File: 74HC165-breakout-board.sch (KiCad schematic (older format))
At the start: 6 parts, among them J1 Conn_01x05, J2 Conn_01x05

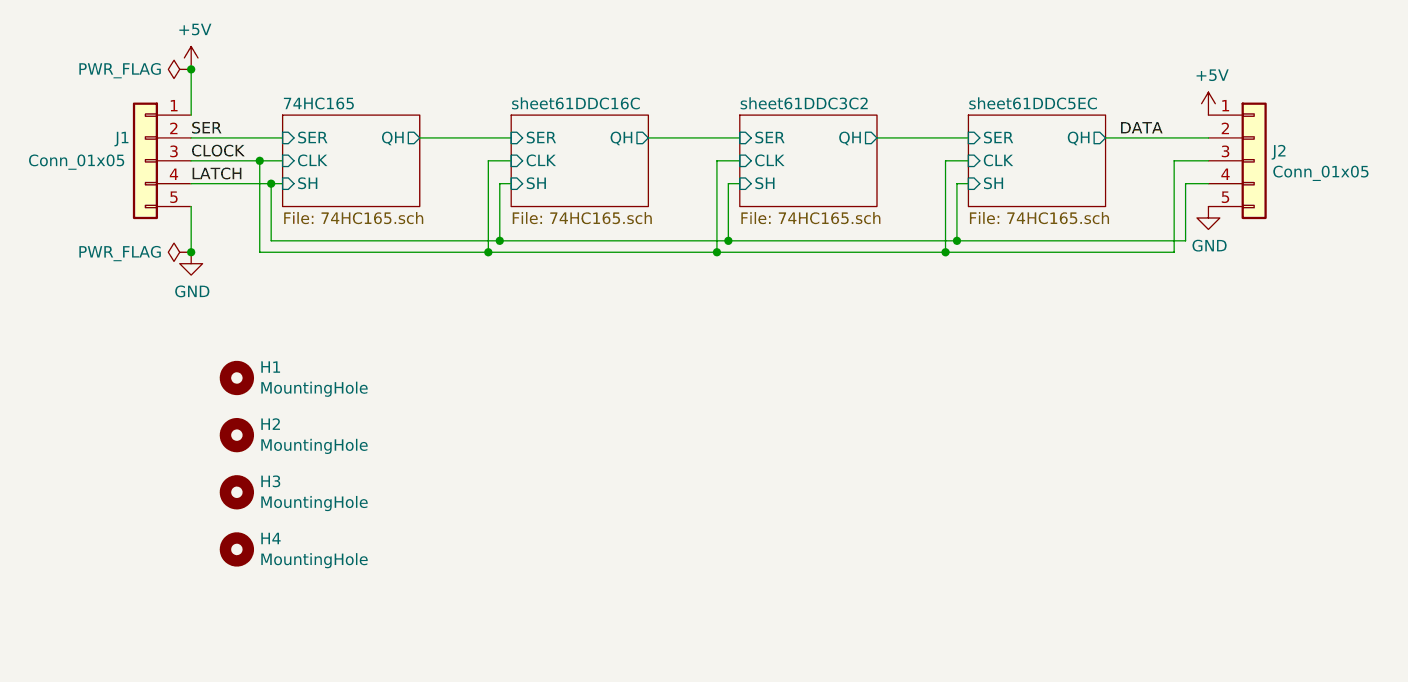
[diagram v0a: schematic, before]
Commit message: Add GND to each header, remove daisy chain
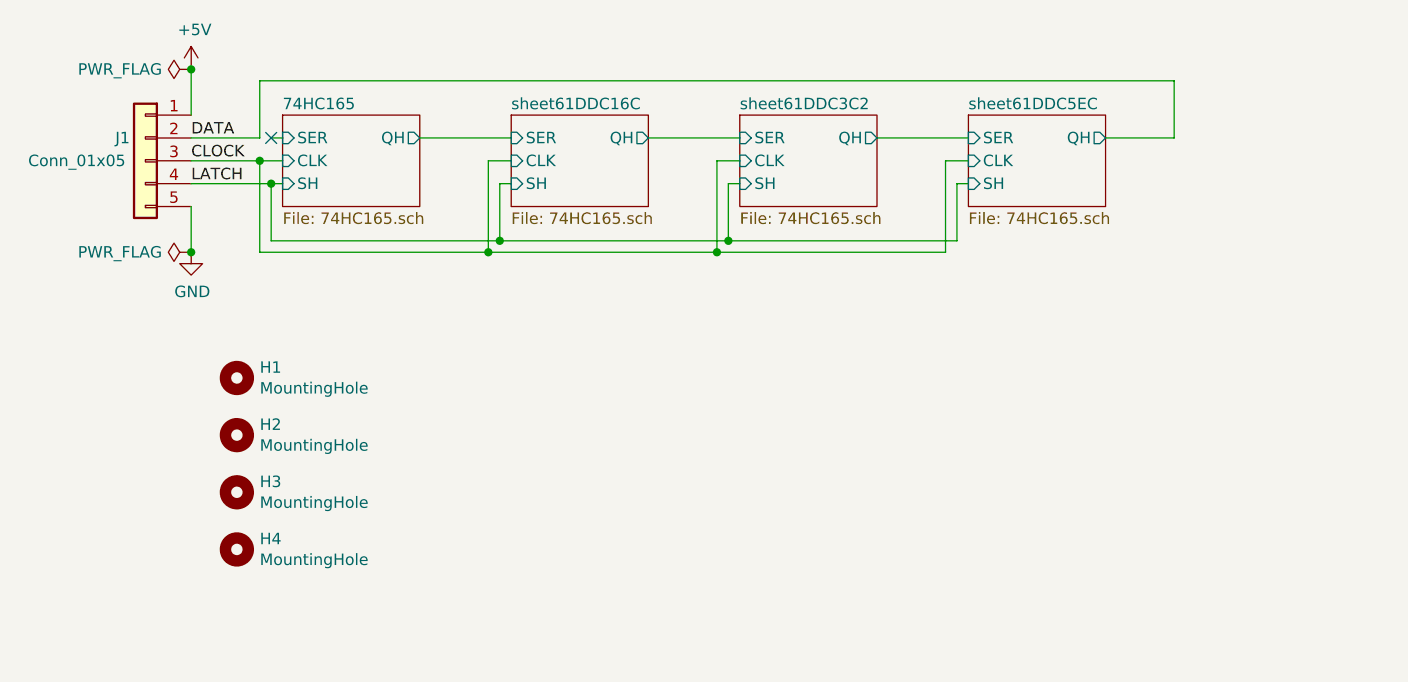
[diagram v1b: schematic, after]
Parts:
- removed J2: Conn_01x05, Connector_JST:JST_XH_B5B-XH-A_1x05_P2.50mm_Vertical, symbol Connector_Generic:Conn_01x05
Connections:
- net SER is gone; now on net DATA: J1.2 (Pin_2)
- no-connect marks 0 -> 1
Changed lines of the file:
@@
 $EndComp
 $Comp
-L power:GND #PWR04
+L power:GND #PWR02
 U 1 1 61DD9981
 P 1300 1500
-F 0 "#PWR04" H 1300 1250 50  0001 C CNN
+F 0 "#PWR02" H 1300 1250 50  0001 C CNN
 F 1 "GND" H 1305 1327 50  0000 C CNN
 F 2 "" H 1300 1500 50  0001 C CNN
@@
 Connection ~ 3600 1500
 $Comp
-L Connector_Generic:Conn_01x05 J2
-U 1 1 61DDF5C9
-P 5950 1100
-F 0 "J2" H 6030 1142 50  0000 L CNN
-F 1 "Conn_01x05" H 6030 1051 50  0000 L CNN
-F 2 "Connector_JST:JST_XH_B5B-XH-A_1x05_P2.50mm_Vertical" H 5950 1100 50  0001 C CNN
-F 3 "~" H 5950 1100 50  0001 C CNN
-	1    5950 1100
-	1    0    0    -1
-$EndComp
-$Comp
-L power:+5V #PWR02
-U 1 1 61DE0AC2
-P 5750 900
-F 0 "#PWR02" H 5750 750 50  0001 C CNN
-F 1 "+5V" H 5765 1073 50  0000 C CNN
-F 2 "" H 5750 900 50  0001 C CNN
-F 3 "" H 5750 900 50  0001 C CNN
-	1    5750 900
-	1    0    0    -1
-$EndComp
-$Comp
-L power:GND #PWR03
-U 1 1 61DE0CBC
-P 5750 1300
-F 0 "#PWR03" H 5750 1050 50  0001 C CNN
-F 1 "GND" H 5755 1127 50  0000 C CNN
-F 2 "" H 5750 1300 50  0001 C CNN
-F 3 "" H 5750 1300 50  0001 C CNN
-	1    5750 1300
-	1    0    0    -1
-$EndComp
-Wire Wire Line
-	4600 1500 5600 1500
-Connection ~ 4600 1500
-Connection ~ 4650 1450
-$Comp
-L power:PWR_FLAG #FLG0101
+L power:PWR_FLAG #FLG01
 U 1 1 61DE2F11
 P 1300 700
-F 0 "#FLG0101" H 1300 775 50  0001 C CNN
+F 0 "#FLG01" H 1300 775 50  0001 C CNN
 F 1 "PWR_FLAG" V 1300 827 50  0000 L CNN
 F 2 "" H 1300 700 50  0001 C CNN
@@
 $EndComp
 Connection ~ 1300 700
-Text Label 5550 1000 2    50   ~ 0
-DATA
-$Comp
-L power:PWR_FLAG #FLG0102
+$Comp
+L power:PWR_FLAG #FLG02
 U 1 1 61DE455D
 P 1300 1500
-F 0 "#FLG0102" H 1300 1575 50  0001 C CNN
+F 0 "#FLG02" H 1300 1575 50  0001 C CNN
 F 1 "PWR_FLAG" V 1300 1627 50  0000 L CNN
 F 2 "" H 1300 1500 50  0001 C CNN
@@
 	1    0    0    -1
 $EndComp
-Wire Wire Line
-	5300 1000 5750 1000
-Wire Wire Line
-	5650 1450 5650 1200
-Wire Wire Line
-	5650 1200 5750 1200
-Wire Wire Line
-	4650 1450 5650 1450
-Wire Wire Line
-	5600 1500 5600 1100
-Wire Wire Line
-	5600 1100 5750 1100
 $Comp
 L Connector_Generic:Conn_01x05 J1
@@
 	-1   0    0    -1
 $EndComp
-Wire Wire Line
-	1300 1000 1700 1000
 Text Label 1300 1000 0    50   ~ 0
-SER
+DATA
 Wire Wire Line
 	1300 700  1300 900
+Wire Wire Line
+	1300 1000 1600 1000
+Wire Wire Line
+	1600 1000 1600 750
+Wire Wire Line
+	1600 750  5600 750
+Wire Wire Line
+	5600 750  5600 1000
+Wire Wire Line
+	5600 1000 5300 1000
+Wire Wire Line
+	1650 1000 1700 1000
+NoConn ~ 1650 1000
 $EndSCHEMATC

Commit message: Fix resistors, add tooling holes, add test points
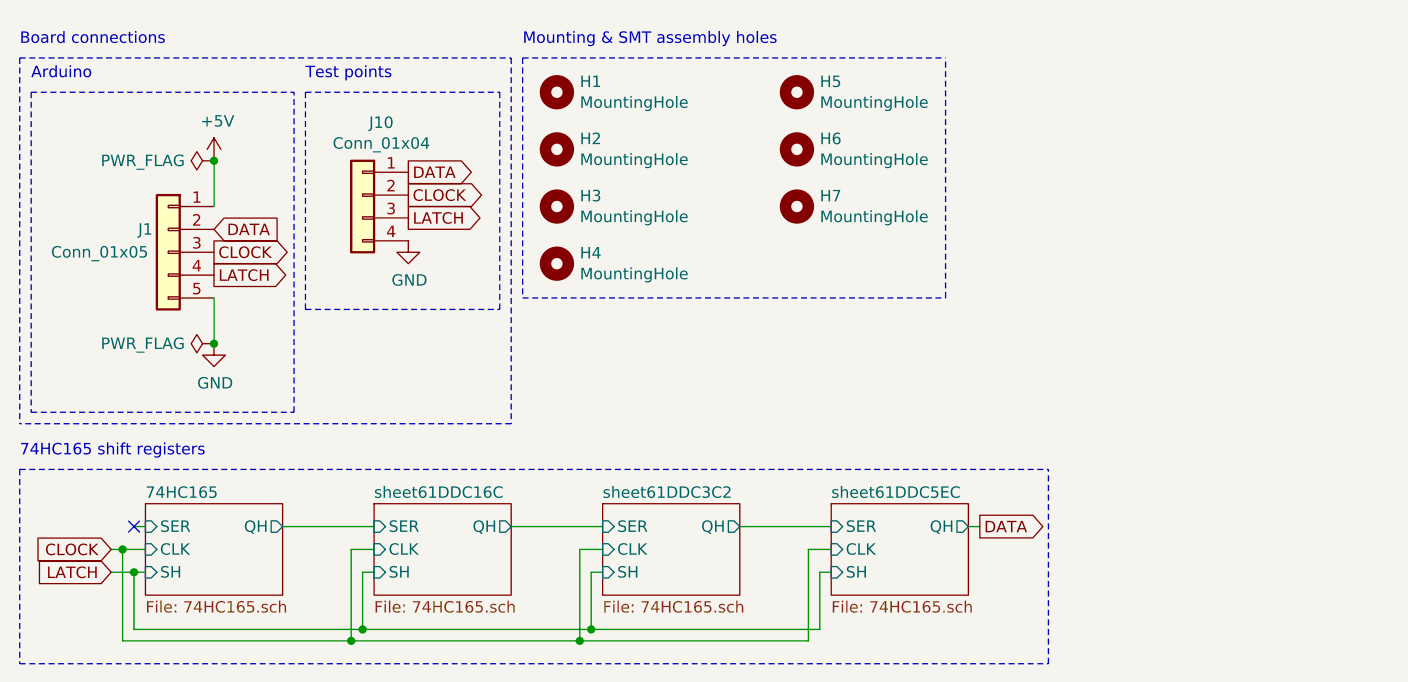
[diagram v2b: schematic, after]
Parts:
- added H5, H6, H7: MountingHole, 74HC165-breakout-board:JLCPCB_Tooling_Hole, symbol Mechanical:MountingHole
- added J10: Conn_01x04, Connector_PinHeader_2.54mm:PinHeader_1x04_P2.54mm_Vertical, symbol Connector_Generic:Conn_01x04
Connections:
- net CLOCK: now also J10.2 (Pin_2)
- net DATA: now also J10.1 (Pin_1)
- net GND: now also J10.4 (Pin_4)
- net LATCH: now also J10.3 (Pin_3)
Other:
- note added: "74HC165 shift registers"
- note added: "Arduino"
- note added: "Board connections"
- note added: "Mounting & SMT assembly holes"
- note added: "Test points"
- moved on the sheet: H1, H2, H3, H4, J1

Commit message: Put ground on pin 1 of all the connectors Fixes #1
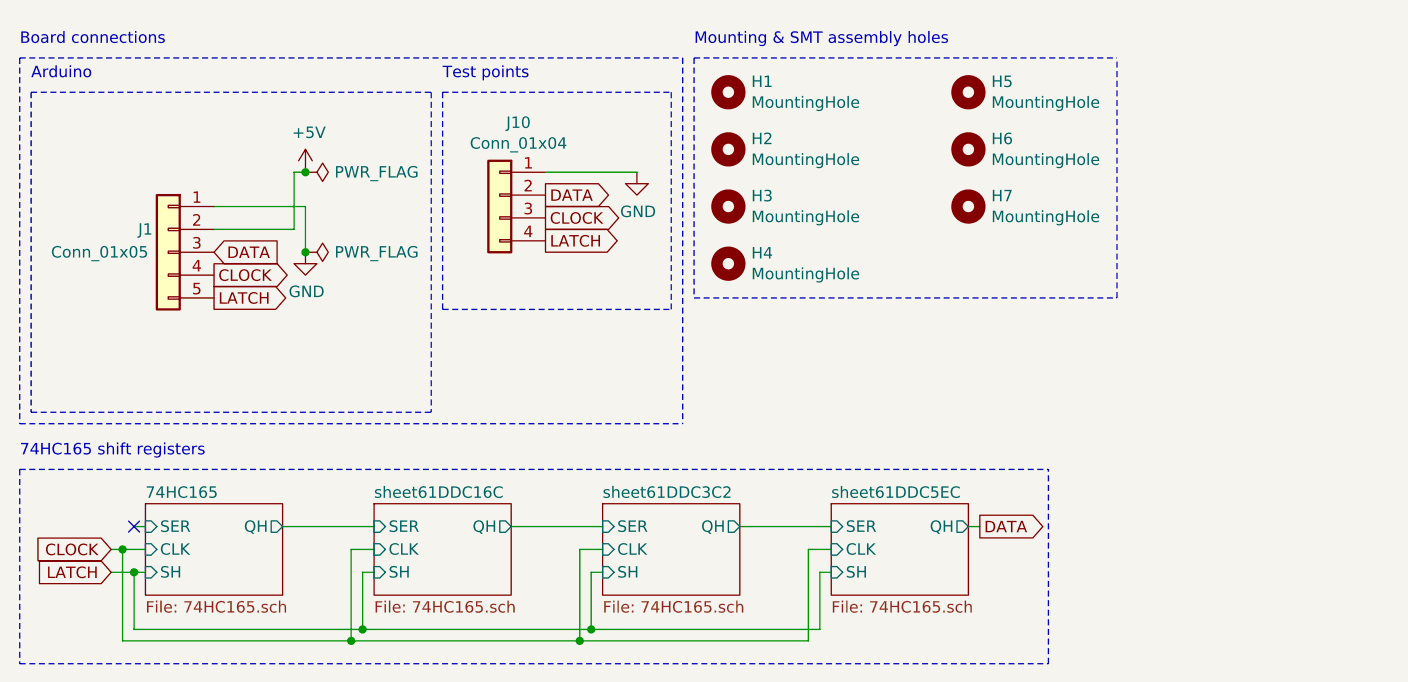
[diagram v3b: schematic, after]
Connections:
- net +5V: now also J1.2 (Pin_2); no longer J1.1 (Pin_1)
- net CLOCK: now also J1.4 (Pin_4), J10.3 (Pin_3); no longer J1.3 (Pin_3), J10.2 (Pin_2)
- net DATA: now also J1.3 (Pin_3), J10.2 (Pin_2); no longer J1.2 (Pin_2), J10.1 (Pin_1)
- net GND: now also J1.1 (Pin_1), J10.1 (Pin_1); no longer J1.5 (Pin_5), J10.4 (Pin_4)
- net LATCH: now also J1.5 (Pin_5), J10.4 (Pin_4); no longer J1.4 (Pin_4), J10.3 (Pin_3)
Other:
- moved on the sheet: H1, H2, H3, H4, H5, H6, H7, J10
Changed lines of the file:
@@
 L power:+5V #PWR01
 U 1 1 61DD970E
-P 1400 1100
-F 0 "#PWR01" H 1400 950 50  0001 C CNN
-F 1 "+5V" H 1415 1273 50  0000 C CNN
-F 2 "" H 1400 1100 50  0001 C CNN
-F 3 "" H 1400 1100 50  0001 C CNN
-	1    1400 1100
+P 1800 1150
+F 0 "#PWR01" H 1800 1000 50  0001 C CNN
+F 1 "+5V" H 1815 1323 50  0000 C CNN
+F 2 "" H 1800 1150 50  0001 C CNN
+F 3 "" H 1800 1150 50  0001 C CNN
+	1    1800 1150
 	1    0    0    -1
 $EndComp
@@
 L power:GND #PWR02
 U 1 1 61DD9981
-P 1400 1900
-F 0 "#PWR02" H 1400 1650 50  0001 C CNN
-F 1 "GND" H 1405 1727 50  0000 C CNN
-F 2 "" H 1400 1900 50  0001 C CNN
-F 3 "" H 1400 1900 50  0001 C CNN
-	1    1400 1900
+P 1800 1500
+F 0 "#PWR02" H 1800 1250 50  0001 C CNN
+F 1 "GND" H 1805 1327 50  0000 C CNN
+F 2 "" H 1800 1500 50  0001 C CNN
+F 3 "" H 1800 1500 50  0001 C CNN
+	1    1800 1500
 	1    0    0    -1
 $EndComp
@@
 L power:PWR_FLAG #FLG01
 U 1 1 61DE2F11
-P 1400 1100
-F 0 "#FLG01" H 1400 1175 50  0001 C CNN
-F 1 "PWR_FLAG" V 1400 1227 50  0000 L CNN
-F 2 "" H 1400 1100 50  0001 C CNN
-F 3 "~" H 1400 1100 50  0001 C CNN
-	1    1400 1100
-	0    -1   -1   0
-$EndComp
-Connection ~ 1400 1100
+P 1800 1150
+F 0 "#FLG01" H 1800 1225 50  0001 C CNN
+F 1 "PWR_FLAG" V 1800 1277 50  0000 L CNN
+F 2 "" H 1800 1150 50  0001 C CNN
+F 3 "~" H 1800 1150 50  0001 C CNN
+	1    1800 1150
+	0    1    1    0
+$EndComp
 $Comp
 L power:PWR_FLAG #FLG02
 U 1 1 61DE455D
-P 1400 1900
-F 0 "#FLG02" H 1400 1975 50  0001 C CNN
-F 1 "PWR_FLAG" V 1400 2027 50  0000 L CNN
-F 2 "" H 1400 1900 50  0001 C CNN
-F 3 "~" H 1400 1900 50  0001 C CNN
-	1    1400 1900
-	0    -1   -1   0
-$EndComp
-Wire Wire Line
-	1400 1900 1400 1700
-Connection ~ 1400 1900
+P 1800 1500
+F 0 "#FLG02" H 1800 1575 50  0001 C CNN
+F 1 "PWR_FLAG" V 1800 1627 50  0000 L CNN
+F 2 "" H 1800 1500 50  0001 C CNN
+F 3 "~" H 1800 1500 50  0001 C CNN
+	1    1800 1500
+	0    1    1    0
+$EndComp
+Wire Wire Line
+	1800 1500 1800 1300
+Connection ~ 1800 1500
 $Comp
 L Mechanical:MountingHole H1
 U 1 1 61DD1A11
-P 2900 800
-F 0 "H1" H 3000 846 50  0000 L CNN
-F 1 "MountingHole" H 3000 755 50  0000 L CNN
-F 2 "MountingHole:MountingHole_3.2mm_M3" H 2900 800 50  0001 C CNN
-F 3 "~" H 2900 800 50  0001 C CNN
-	1    2900 800
+P 3650 800
+F 0 "H1" H 3750 846 50  0000 L CNN
+F 1 "MountingHole" H 3750 755 50  0000 L CNN
+F 2 "MountingHole:MountingHole_3.2mm_M3" H 3650 800 50  0001 C CNN
+F 3 "~" H 3650 800 50  0001 C CNN
+	1    3650 800
 	1    0    0    -1
 $EndComp
@@
 L Mechanical:MountingHole H2
 U 1 1 61DD1C43
-P 2900 1050
-F 0 "H2" H 3000 1096 50  0000 L CNN
-F 1 "MountingHole" H 3000 1005 50  0000 L CNN
-F 2 "MountingHole:MountingHole_3.2mm_M3" H 2900 1050 50  0001 C CNN
-F 3 "~" H 2900 1050 50  0001 C CNN
-	1    2900 1050
+P 3650 1050
+F 0 "H2" H 3750 1096 50  0000 L CNN
+F 1 "MountingHole" H 3750 1005 50  0000 L CNN
+F 2 "MountingHole:MountingHole_3.2mm_M3" H 3650 1050 50  0001 C CNN
+F 3 "~" H 3650 1050 50  0001 C CNN
+	1    3650 1050
 	1    0    0    -1
 $EndComp
@@
 L Mechanical:MountingHole H3
 U 1 1 61DD1DC1
-P 2900 1300
-F 0 "H3" H 3000 1346 50  0000 L CNN
-F 1 "MountingHole" H 3000 1255 50  0000 L CNN
-F 2 "MountingHole:MountingHole_3.2mm_M3" H 2900 1300 50  0001 C CNN
-F 3 "~" H 2900 1300 50  0001 C CNN
-	1    2900 1300
+P 3650 1300
+F 0 "H3" H 3750 1346 50  0000 L CNN
+F 1 "MountingHole" H 3750 1255 50  0000 L CNN
+F 2 "MountingHole:MountingHole_3.2mm_M3" H 3650 1300 50  0001 C CNN
+F 3 "~" H 3650 1300 50  0001 C CNN
+	1    3650 1300
 	1    0    0    -1
 $EndComp
@@
 L Mechanical:MountingHole H4
 U 1 1 61DD206B
-P 2900 1550
-F 0 "H4" H 3000 1596 50  0000 L CNN
-F 1 "MountingHole" H 3000 1505 50  0000 L CNN
-F 2 "MountingHole:MountingHole_3.2mm_M3" H 2900 1550 50  0001 C CNN
-F 3 "~" H 2900 1550 50  0001 C CNN
-	1    2900 1550
+P 3650 1550
+F 0 "H4" H 3750 1596 50  0000 L CNN
+F 1 "MountingHole" H 3750 1505 50  0000 L CNN
+F 2 "MountingHole:MountingHole_3.2mm_M3" H 3650 1550 50  0001 C CNN
+F 3 "~" H 3650 1550 50  0001 C CNN
+	1    3650 1550
 	1    0    0    -1
 $EndComp
@@
 $EndComp
 Wire Wire Line
-	1400 1100 1400 1300
-Wire Wire Line
 	1050 2700 1100 2700
 NoConn ~ 1050 2700
@@
 L Mechanical:MountingHole H5
 U 1 1 61DD6D8A
-P 3950 800
-F 0 "H5" H 4050 846 50  0000 L CNN
-F 1 "MountingHole" H 4050 755 50  0000 L CNN
-F 2 "74HC165-breakout-board:JLCPCB_Tooling_Hole" H 3950 800 50  0001 C CNN
-F 3 "~" H 3950 800 50  0001 C CNN
-	1    3950 800
+P 4700 800
+F 0 "H5" H 4800 846 50  0000 L CNN
+F 1 "MountingHole" H 4800 755 50  0000 L CNN
+F 2 "74HC165-breakout-board:JLCPCB_Tooling_Hole" H 4700 800 50  0001 C CNN
+F 3 "~" H 4700 800 50  0001 C CNN
+	1    4700 800
 	1    0    0    -1
 $EndComp
@@
 L Mechanical:MountingHole H6
 U 1 1 61DD7089
-P 3950 1050
-F 0 "H6" H 4050 1096 50  0000 L CNN
-F 1 "MountingHole" H 4050 1005 50  0000 L CNN
-F 2 "74HC165-breakout-board:JLCPCB_Tooling_Hole" H 3950 1050 50  0001 C CNN
-F 3 "~" H 3950 1050 50  0001 C CNN
-	1    3950 1050
+P 4700 1050
+F 0 "H6" H 4800 1096 50  0000 L CNN
+F 1 "MountingHole" H 4800 1005 50  0000 L CNN
+F 2 "74HC165-breakout-board:JLCPCB_Tooling_Hole" H 4700 1050 50  0001 C CNN
+F 3 "~" H 4700 1050 50  0001 C CNN
+	1    4700 1050
 	1    0    0    -1
 $EndComp
@@
 L Mechanical:MountingHole H7
 U 1 1 61DD7204
-P 3950 1300
-F 0 "H7" H 4050 1346 50  0000 L CNN
-F 1 "MountingHole" H 4050 1255 50  0000 L CNN
-F 2 "74HC165-breakout-board:JLCPCB_Tooling_Hole" H 3950 1300 50  0001 C CNN
-F 3 "~" H 3950 1300 50  0001 C CNN
-	1    3950 1300
-	1    0    0    -1
-$EndComp
-Wire Notes Line
-	2750 650  2750 1700
-Wire Notes Line
-	2750 1700 4600 1700
-Wire Notes Line
-	4600 1700 4600 650
-Wire Notes Line
-	2750 650  4600 650
-Text Notes 2750 600  0    50   ~ 0
+P 4700 1300
+F 0 "H7" H 4800 1346 50  0000 L CNN
+F 1 "MountingHole" H 4800 1255 50  0000 L CNN
+F 2 "74HC165-breakout-board:JLCPCB_Tooling_Hole" H 4700 1300 50  0001 C CNN
+F 3 "~" H 4700 1300 50  0001 C CNN
+	1    4700 1300
+	1    0    0    -1
+$EndComp
+Wire Notes Line
+	3500 650  3500 1700
+Wire Notes Line
+	3500 1700 5350 1700
+Wire Notes Line
+	5350 1700 5350 650
+Wire Notes Line
+	3500 650  5350 650
+Text Notes 3500 600  0    50   ~ 0
 Mounting & SMT assembly holes
 Text Notes 550  600  0    50   ~ 0
 Board connections
-Text GLabel 1400 1400 2    50   Input ~ 0
+Text GLabel 1400 1500 2    50   Input ~ 0
 DATA
-Text GLabel 1400 1500 2    50   Output ~ 0
+Text GLabel 1400 1600 2    50   Output ~ 0
 CLOCK
-Text GLabel 1400 1600 2    50   Output ~ 0
+Text GLabel 1400 1700 2    50   Output ~ 0
 LATCH
 Text GLabel 4750 2700 2    50   Output ~ 0
@@
 L Connector_Generic:Conn_01x04 J10
 U 1 1 61DEB799
-P 2050 1250
-F 0 "J10" H 1968 1567 50  0000 C CNN
-F 1 "Conn_01x04" H 1968 1476 50  0000 C CNN
-F 2 "Connector_PinHeader_2.54mm:PinHeader_1x04_P2.54mm_Vertical" H 2050 1250 50  0001 C CNN
-F 3 "~" H 2050 1250 50  0001 C CNN
-	1    2050 1250
+P 2650 1250
+F 0 "J10" H 2568 1567 50  0000 C CNN
+F 1 "Conn_01x04" H 2568 1476 50  0000 C CNN
+F 2 "Connector_PinHeader_2.54mm:PinHeader_1x04_P2.54mm_Vertical" H 2650 1250 50  0001 C CNN
+F 3 "~" H 2650 1250 50  0001 C CNN
+	1    2650 1250
 	-1   0    0    -1
 $EndComp
-Text GLabel 2250 1150 2    50   Output ~ 0
+Text GLabel 2850 1250 2    50   Output ~ 0
 DATA
-Text GLabel 2250 1250 2    50   Output ~ 0
+Text GLabel 2850 1350 2    50   Output ~ 0
 CLOCK
-Text GLabel 2250 1350 2    50   Output ~ 0
+Text GLabel 2850 1450 2    50   Output ~ 0
 LATCH
 $Comp
 L power:GND #PWR0105
 U 1 1 61DECCBA
-P 2250 1450
-F 0 "#PWR0105" H 2250 1200 50  0001 C CNN
-F 1 "GND" H 2255 1277 50  0000 C CNN
-F 2 "" H 2250 1450 50  0001 C CNN
-F 3 "" H 2250 1450 50  0001 C CNN
-	1    2250 1450
+P 3250 1150
+F 0 "#PWR0105" H 3250 900 50  0001 C CNN
+F 1 "GND" H 3255 977 50  0000 C CNN
+F 2 "" H 3250 1150 50  0001 C CNN
+F 3 "" H 3250 1150 50  0001 C CNN
+	1    3250 1150
 	1    0    0    -1
 $EndComp
 Text Notes 600  750  0    50   ~ 0
 Arduino
-Text Notes 1800 750  0    50   ~ 0
+Text Notes 2400 750  0    50   ~ 0
 Test points
 Wire Notes Line
 	600  800  600  2200
 Wire Notes Line
-	600  2200 1750 2200
-Wire Notes Line
-	1750 2200 1750 800
-Wire Notes Line
-	600  800  1750 800
-Wire Notes Line
-	1800 800  2650 800
-Wire Notes Line
-	2650 800  2650 1750
-Wire Notes Line
-	1800 1750 2650 1750
-Wire Notes Line
-	1800 800  1800 1750
-Wire Notes Line
-	550  650  2700 650
-Wire Notes Line
-	2700 650  2700 2250
-Wire Notes Line
-	2700 2250 550  2250
+	3400 800  3400 1750
+Wire Notes Line
+	2400 800  2400 1750
+Wire Notes Line
+	3450 650  3450 2250
 Wire Notes Line
 	550  650  550  2250
@@
 Text Notes 550  2400 0    50   ~ 0
 74HC165 shift registers
+Wire Wire Line
+	1400 1300 1800 1300
+Wire Wire Line
+	1400 1400 1750 1400
+Wire Wire Line
+	1750 1400 1750 1150
+Wire Wire Line
+	1750 1150 1800 1150
+Connection ~ 1800 1150
+Wire Notes Line
+	600  800  2350 800
+Wire Notes Line
+	2350 800  2350 2200
+Wire Notes Line
+	600  2200 2350 2200
+Wire Wire Line
+	2850 1150 3250 1150
+Wire Notes Line
+	2400 800  3400 800
+Wire Notes Line
+	2400 1750 3400 1750
+Wire Notes Line
+	550  2250 3450 2250
+Wire Notes Line
+	550  650  3450 650
 $EndSCHEMATC
